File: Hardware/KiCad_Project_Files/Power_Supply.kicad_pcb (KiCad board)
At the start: 2 copper layers, 100 x 50 mm, 103 parts, among them J2 Conn_01x01, J3 Conn_01x01, J4 Screw_Terminal_01x02, J5 USB_C_Receptacle_USB2.0, Q1 FDN335N, Q2 FDN335N, SW1 UP, SW2 DW, SW3 V_I_SEL, SW4 O_EN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

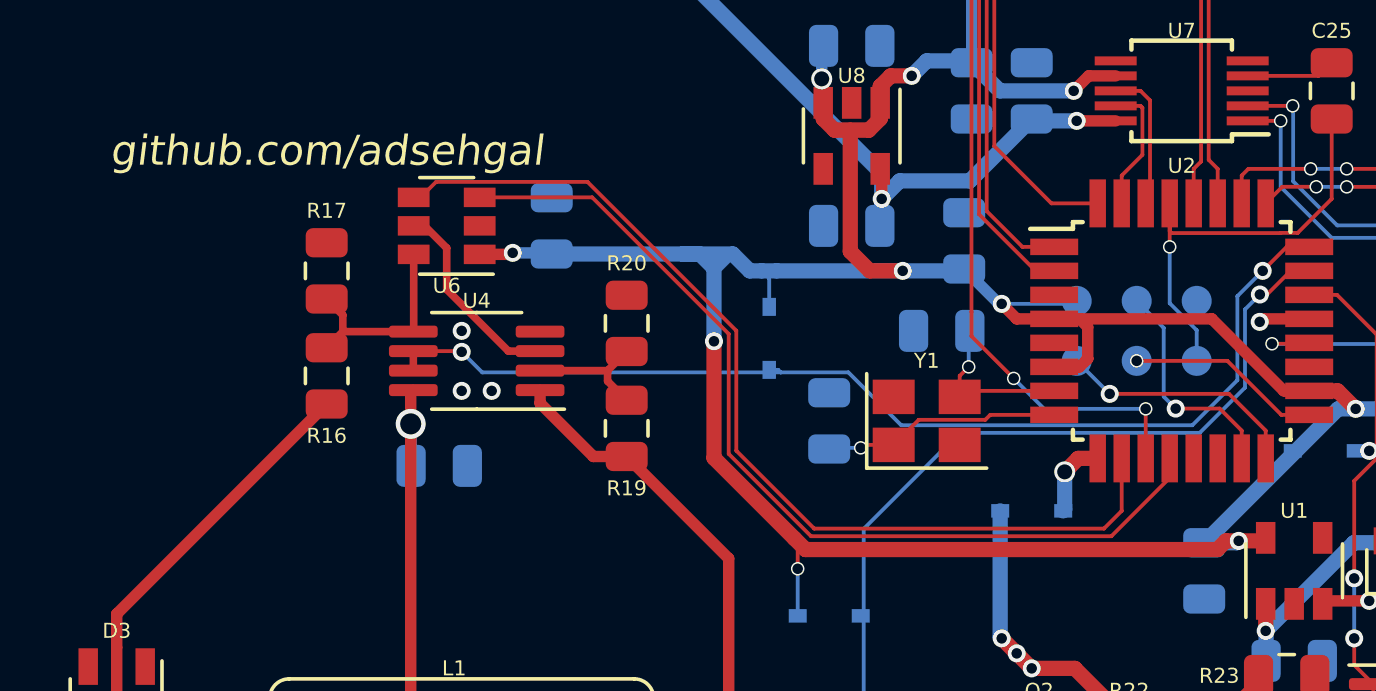
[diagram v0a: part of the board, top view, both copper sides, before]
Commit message: added high voltage digi_pot control
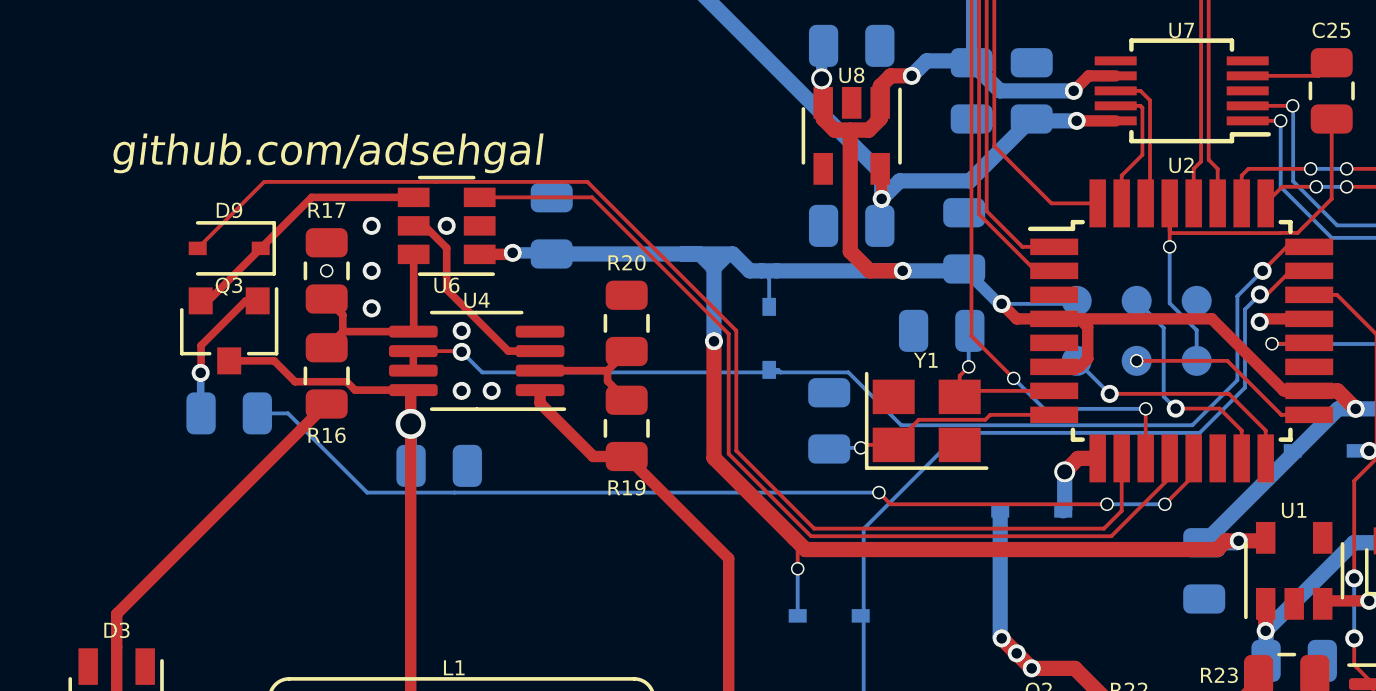
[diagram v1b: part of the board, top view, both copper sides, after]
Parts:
- added D9: CUS10S30, Diode_SMD:D_SOD-323, F.Cu at (59.8, 30.2)
- added Q3: FDN335N, Package_TO_SOT_SMD:SOT-23, F.Cu at (59.8, 33.0)
- added R25: 1K, Resistor_SMD:R_0805_2012Metric, B.Cu at (59.8, 35.8)
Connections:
- U2 pad 13: (no net) -> /POT_VIHH
- U6 pad 4: /~POT_CS -> Net-(D9-Pad1)
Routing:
- net /POT_VIHH: track 0.00 -> 33.4 mm, vias 0 -> 3
- net Net-(D9-Pad1): track 0.00 -> 8.76 mm
- net /~POT_CS: track 32.9 -> 40.8 mm
- net +VSW: track 68.9 -> 75.4 mm
- net Net-(Q3-Pad1): track 0.00 -> 4.78 mm, vias 0 -> 1
- net GND: vias 134 -> 139
